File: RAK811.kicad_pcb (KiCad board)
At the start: 2 copper layers, 27.5 x 46.5 mm, 63 parts, among them J1 CONN_01X01, P1 CONN_01X02, P2 CONN_01X03, P3 CONN_01X06, P4 CONN_01X14, P5 CONN_01X14, U1 RAK811

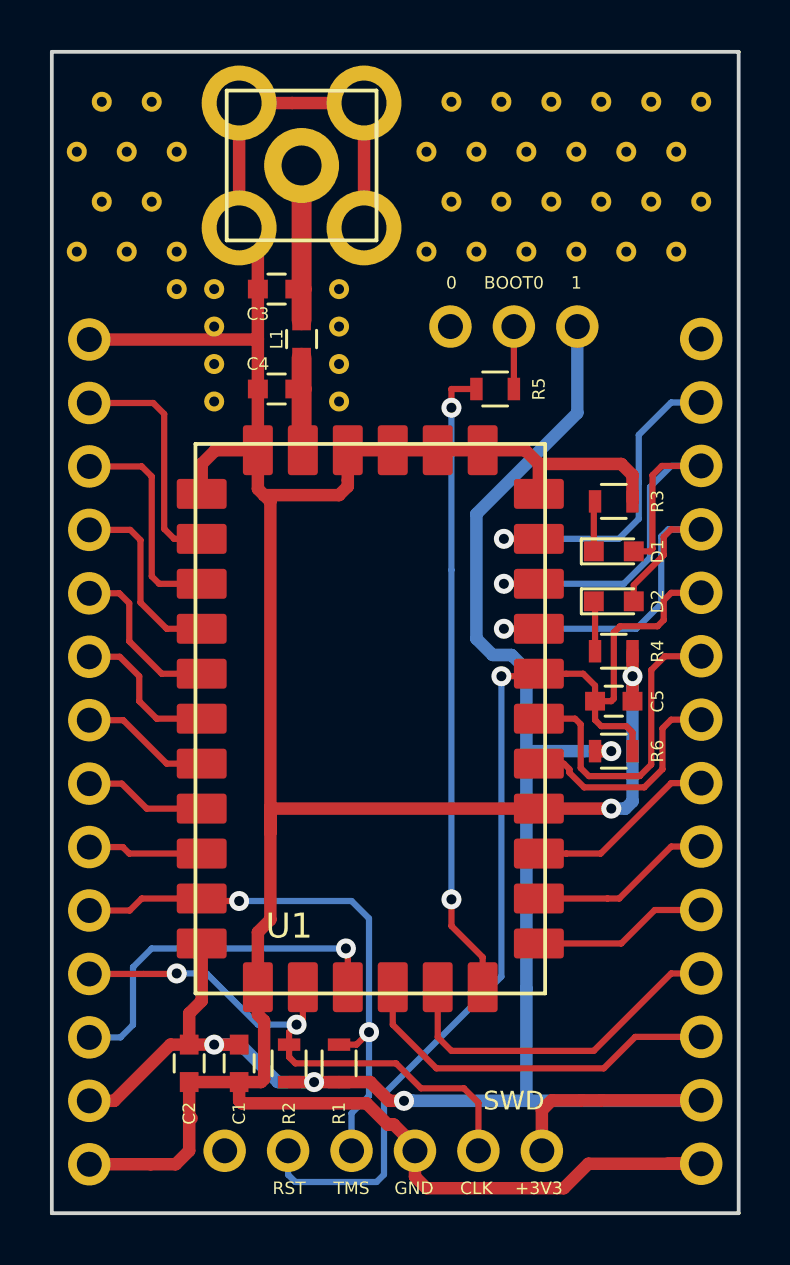
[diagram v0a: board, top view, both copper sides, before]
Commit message: Added IPX + Regulator
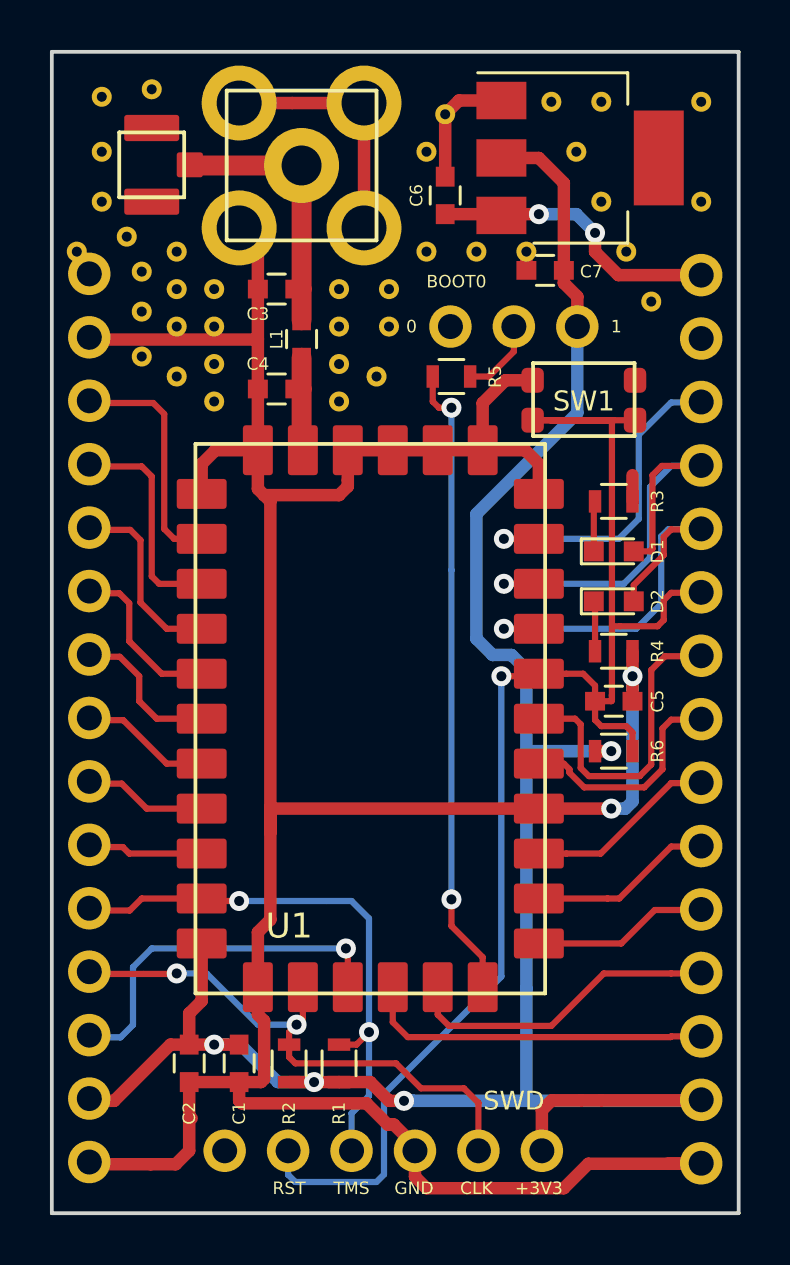
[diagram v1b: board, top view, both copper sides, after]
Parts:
- removed the J1 at (74.0, 47.0)
- removed the J1 at (73.0, 45.0)
- removed the J1 at (74.0, 43.0)
- removed the J1 at (73.0, 41.0)
- removed the J1 at (72.0, 43.0)
- removed the J1 at (70.0, 47.0)
- removed the J1 at (69.0, 45.0)
- removed the J1 at (67.0, 41.0)
- removed the J1 at (68.0, 43.0)
- removed the J1 at (66.0, 43.0)
- removed the J1 at (67.0, 45.0)
- removed the J1 at (65.0, 45.0)
- removed the J1 at (65.0, 41.0)
- removed the J1 at (53.0, 45.0)
- removed the J1 at (52.0, 43.0)
- removed the J1 at (54.0, 43.0)
- removed the J1 at (53.0, 41.0)
- added C6: 22uF, Capacitors_SMD:C_0603, F.Cu at (64.8, 44.8)
- added C7: 22uF, Capacitors_SMD:C_0603, F.Cu at (68.8, 47.8)
- added J1: CONN_01X01, pad:duko, F.Cu at (52.0, 46.4)
- added J1: CONN_01X01, pad:duko, F.Cu at (62.5, 48.5)
- added J1: CONN_01X01, pad:duko, F.Cu at (53.0, 40.5)
- added J1: CONN_01X01, pad:duko, F.Cu at (54.0, 52.0)
- added J1: CONN_01X01, pad:duko, F.Cu at (54.0, 50.0)
- added J1: CONN_01X01, pad:duko, F.Cu at (52.6, 51.2)
- added J1: CONN_01X01, pad:duko, F.Cu at (52.6, 49.4)
- added J1: CONN_01X01, pad:duko, F.Cu at (62.0, 52.0)
- added J1: CONN_01X01, pad:duko, F.Cu at (73.0, 49.0)
- added J1: CONN_01X01, pad:duko, F.Cu at (64.8, 41.5)
- added J1: CONN_01X01, pad:duko, F.Cu at (62.5, 50.0)
- added P6: CONN_01X02, ipx:ipx, F.Cu at (53.0, 43.5)
- added SW1: SW_SPST_Small, KMR241NG:KMR241NG, F.Cu at (70.3, 53.8)
- added U2: LD1117S12CTR, TO_SOT_Packages_SMD:SOT-223, F.Cu at (70.2, 43.2)
- P4, P5: value CONN_01X14 -> CONN_01X15; footprint special_headers:Pin_Header_Straight_1x14_Pitch2.54mm -> special_headers:Pin_Header_Straight_1x15_Pitch2.54mm
- moved P5 35.6 mm to (75.0, 47.9), turned to 0 degrees
- moved R5 1.82 mm to (65.0, 52.0)
- moved J1 1.00 mm to (51.0, 43.0)
- moved J1 1.00 mm to (52.6, 47.8)
- moved J1 0.20 mm to (51.0, 40.8)
- moved P4 0.09 mm to (50.5, 83.5)
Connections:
- P5 pad 1: GND -> +5V
- P5 pad 10: RST -> PB9
- P5 pad 11: PB10 -> PB8
- P5 pad 12: PB11 -> PB5
- P5 pad 13: PB2 -> PB3
- P5 pad 14: GND -> +3V3
- P5 pad 2: +3V3 -> GND
- P5 pad 3: PB3 -> PB2
- P5 pad 4: PB5 -> PB11
- P5 pad 5: PB8 -> PB10
- P5 pad 6: PB9 -> RST
- P5 pad 7: PA2 -> UART2_TXD
- P5 pad 9: UART2_TXD -> PA2
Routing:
- net RST: track 43.0 -> 61.5 mm
- net +5V: track 0.00 -> 11.7 mm, vias 0 -> 2
- net +3V3: track 79.0 -> 87.9 mm
- net Net-(C3-Pad1): track 6.15 -> 10.6 mm
- net PB5: track 14.1 -> 12.7 mm
- net PB3: track 15.1 -> 14.0 mm
- net GND: track 135.5 -> 136.6 mm
- net Net-(P2-Pad2): track 2.50 -> 3.16 mm

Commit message: Added better RF path
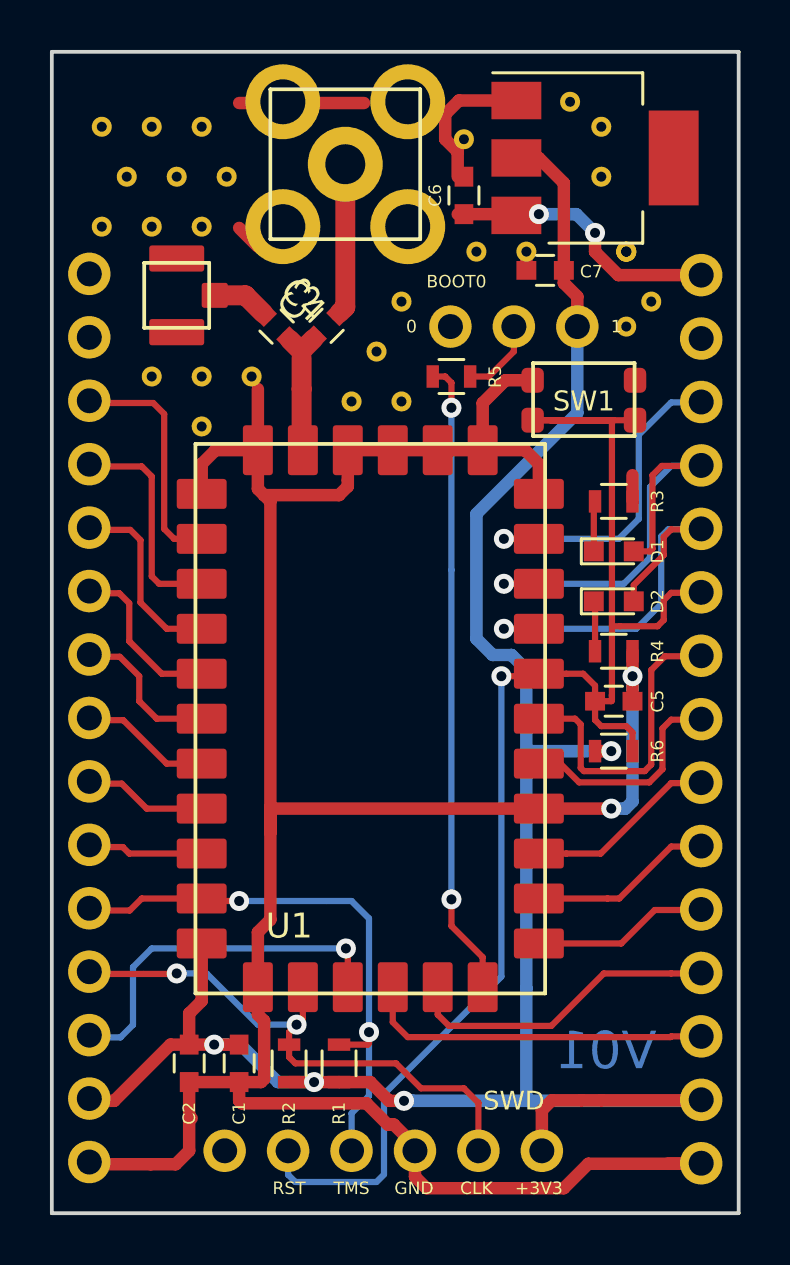
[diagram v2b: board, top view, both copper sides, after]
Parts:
- removed the J1 at (52.0, 46.4)
- removed the J1 at (62.5, 48.5)
- removed the J1 at (53.0, 40.5)
- removed the J1 at (54.0, 48.5)
- removed the J1 at (60.5, 51.5)
- removed the J1 at (55.5, 53.0)
- removed the J1 at (60.5, 48.5)
- removed the J1 at (60.5, 50.0)
- removed the J1 at (60.5, 53.0)
- removed the J1 at (55.5, 51.5)
- removed the J1 at (55.5, 50.0)
- removed the J1 at (54.0, 52.0)
- removed the J1 at (55.5, 48.5)
- removed the J1 at (75.0, 41.0)
- removed the J1 at (75.0, 45.0)
- removed the J1 at (71.0, 41.0)
- removed the J1 at (71.0, 45.0)
- removed the J1 at (70.0, 43.0)
- removed the J1 at (54.0, 50.0)
- removed the J1 at (64.0, 47.0)
- removed the J1 at (64.0, 43.0)
- removed the J1 at (54.0, 47.0)
- removed the J1 at (52.6, 47.8)
- removed the J1 at (50.0, 47.0)
- removed the J1 at (51.0, 45.0)
- removed the J1 at (51.0, 40.8)
- removed the J1 at (52.6, 51.2)
- removed the J1 at (52.6, 49.4)
- removed the J1 at (62.0, 52.0)
- removed the J1 at (64.8, 41.5)
- removed the J1 at (62.5, 50.0)
- removed L1: 10pF C, Capacitors_SMD:C_0603
- added J1: CONN_01X01, pad:duko, F.Cu at (65.5, 42.5)
- added J1: CONN_01X01, pad:duko, F.Cu at (72.0, 50.0)
- added J1: CONN_01X01, pad:duko, F.Cu at (72.0, 47.0)
- added J1: CONN_01X01, pad:duko, F.Cu at (71.0, 44.0)
- added J1: CONN_01X01, pad:duko, F.Cu at (71.0, 42.0)
- added J1: CONN_01X01, pad:duko, F.Cu at (55.0, 42.0)
- added J1: CONN_01X01, pad:duko, F.Cu at (53.0, 42.0)
- added J1: CONN_01X01, pad:duko, F.Cu at (51.0, 42.0)
- added J1: CONN_01X01, pad:duko, F.Cu at (52.0, 44.0)
- added J1: CONN_01X01, pad:duko, F.Cu at (54.0, 44.0)
- added J1: CONN_01X01, pad:duko, F.Cu at (56.0, 44.0)
- added J1: CONN_01X01, pad:duko, F.Cu at (63.0, 49.0)
- added J1: CONN_01X01, pad:duko, F.Cu at (55.0, 46.0)
- added J1: CONN_01X01, pad:duko, F.Cu at (53.0, 46.0)
- added J1: CONN_01X01, pad:duko, F.Cu at (62.0, 51.0)
- added J1: CONN_01X01, pad:duko, F.Cu at (63.0, 53.0)
- added J1: CONN_01X01, pad:duko, F.Cu at (61.0, 53.0)
- added J1: CONN_01X01, pad:duko, F.Cu at (55.0, 54.0)
- added J1: CONN_01X01, pad:duko, F.Cu at (57.0, 52.0)
- added J1: CONN_01X01, pad:duko, F.Cu at (55.0, 52.0)
- added J1: CONN_01X01, pad:duko, F.Cu at (53.0, 52.0)
- moved P6 5.32 mm to (54.0, 48.8)
- moved J1 3.00 mm to (51.0, 46.0)
- moved C4 2.50 mm to (58.0, 50.0), turned to 315 degrees
- moved C3 2.48 mm to (60.0, 50.0), turned to 45 degrees
- moved P1 1.75 mm to (60.8, 43.5)
- moved C6 0.75 mm to (65.5, 44.8)
- moved J1 0.75 mm to (69.8, 41.0)
- moved U2 0.60 mm to (70.8, 43.2)
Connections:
- C3 pad 2: GND -> Net-(C3-Pad2)
- C4 pad 1: GND -> Net-(C4-Pad1)
- C4 pad 2: Net-(C4-Pad2) -> Net-(C3-Pad1)
- P1 pad 1: Net-(C3-Pad1) -> Net-(C3-Pad2)
- P6 pad 1: Net-(C3-Pad1) -> Net-(C4-Pad1)
- U1 pad 33: Net-(C4-Pad2) -> Net-(C3-Pad1)
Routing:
- net GND: track 136.6 -> 119.3 mm
- net Net-(C3-Pad2): track 0.00 -> 6.03 mm
- net Net-(C3-Pad1): track 10.6 -> 5.83 mm
- net Net-(C4-Pad2): track 3.97 -> 0.00 mm
- net Net-(C4-Pad1): track 0.00 -> 2.24 mm
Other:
- board text added: "+5V"
- board text added: "V01"
